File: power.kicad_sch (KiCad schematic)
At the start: 90 parts, among them J6 Molex_Nano-Fit_1x2_105309-2202, Q1 BSS138-7-F, Q2 SI7613DN-T1-GE3, Q3 BSS138-7-F, Q4 SSM3J332R, U18 TPS56C230, U19 TPS56C230, U20 TPS3840PL30DBVR, U21 TPS564247DRLR, U22 TPS564247DRLR, U23 TLV73333PDBVT, U48 INA219AIDCNR, U49 INA219AIDCNR, U50 INA219AIDCNR

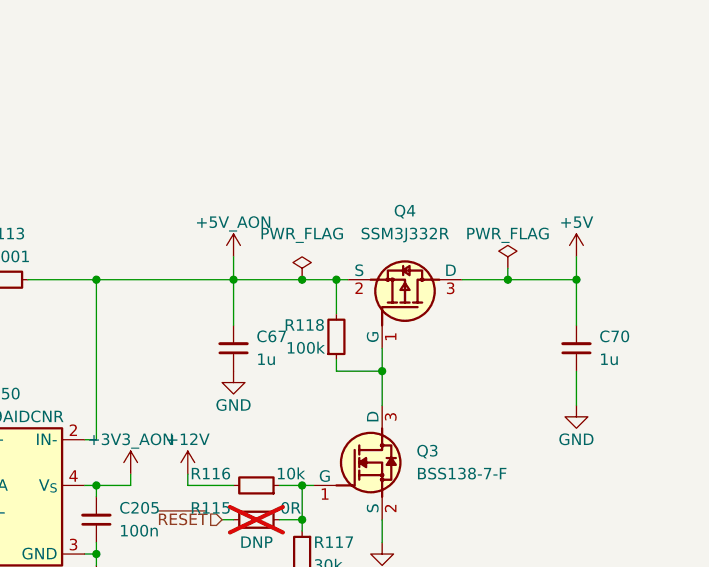
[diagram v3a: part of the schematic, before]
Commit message: [#58904] Change +5V load switch transistor to SI7613DN-T1-GE3
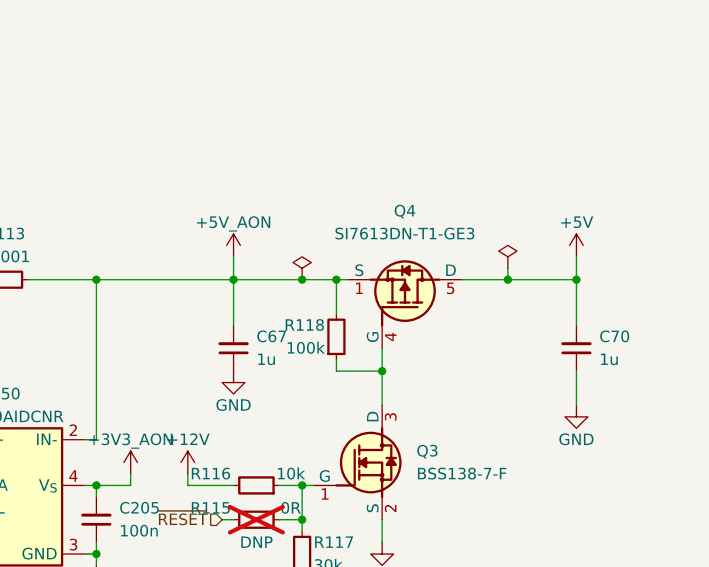
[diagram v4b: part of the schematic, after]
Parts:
- removed Q4: SSM3J332R, antmicro-footprints:SOT-23-3, symbol antmicroTransistorsFETsMOSFETsSingle:SSM3J332R
- added Q4: SI7613DN-T1-GE3, antmicro-footprints:Vishay_PowerPAK_1212-8_Single, symbol antmicroTransistorsFETsMOSFETsSingle:SI7613DN-T1-GE3
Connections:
- net +5V: now also Q4.5 (D)
- net +5V_AON: now also Q4.1 (S), Q4.2 (S), Q4.3 (S)
- net at Q3.3 (D), R118.1: now also Q4.4 (G)
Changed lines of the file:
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@@
     )
     (property "Value" "PWR_FLAG" (at 386.08 50.8 0)
-      (effects (font (size 1.27 1.27)))
+      (effects (font (size 1.27 1.27)) hide)
     )
     (property "Footprint" "" (at 386.08 54.61 0)
@@
     )
     (property "Value" "PWR_FLAG" (at 363.22 50.8 0)
-      (effects (font (size 1.27 1.27)))
+      (effects (font (size 1.27 1.27)) hide)
     )
     (property "Footprint" "" (at 363.22 55.88 0)
@@
     )
   )
+  (symbol (lib_id "antmicroTransistorsFETsMOSFETsSingle:SI7613DN-T1-GE3") (at 372.11 63.5 270) (mirror x) (unit 1)
+    (in_bom yes) (on_board yes) (dnp no) (fields_autoplaced)
+    (property "Reference" "Q4" (at 374.65 48.26 90)
+      (effects (font (size 1.27 1.27) (thickness 0.15)))
+    )
+    (property "Value" "SI7613DN-T1-GE3" (at 374.65 50.8 90)
+      (effects (font (size 1.27 1.27) (thickness 0.15)) hide)
+    )
+    (property "Footprint" "antmicro-footprints:Vishay_PowerPAK_1212-8_Single" (at 373.38 48.26 0)
+      (effects (font (size 1.27 1.27) (thickness 0.15)) (justify left bottom) hide)
+    )
+    (property "Datasheet" "https://www.vishay.com/docs/64809/si7613dn.pdf" (at 370.84 48.26 0)
+      (effects (font (size 1.27 1.27) (thickness 0.15)) (justify left bottom) hide)
+    )
+    (property "MPN" "SI7613DN-T1-GE3" (at 374.65 50.8 90)
+      (effects (font (size 1.27 1.27) (thickness 0.15)))
+    )
+    (property "Manufacturer" "Vishay" (at 364.49 48.26 0)
+      (effects (font (size 1.27 1.27) (thickness 0.15)) (justify left bottom) hide)
+    )
+    (property "Author" "Antmicro" (at 361.95 48.26 0)
+      (effects (font (size 1.27 1.27) (thickness 0.15)) (justify left bottom) hide)
+    )
+    (property "License" "Apache-2.0" (at 359.41 48.26 0)
+      (effects (font (size 1.27 1.27) (thickness 0.15)) (justify left bottom) hide)
+    )
+    (pin "5")
+    (pin "4")
+    (pin "3")
+    (pin "1")
+    (pin "2")
+    (instances
+      (project "com-express-7-baseboard"
+        (path "/1b8c34da-dad5-4b0b-8c4b-45db766c4dfa/9e43a8fe-5590-4346-856e-e8b6e5166965"
+          (reference "Q4") (unit 1)
+        )
+      )
+    )
+  )
   (symbol (lib_id "antmicroPowerMeasurement:INA219AIDCNR") (at 323.85 73.66 0) (unit 1)
     (in_bom yes) (on_board yes) (dnp no)
@@
         )
       )
-    )
-  )
-  (symbol (lib_id "antmicroTransistorsFETsMOSFETsSingle:SSM3J332R") (at 372.11 63.5 270) (mirror x) (unit 1)
-    (in_bom yes) (on_board yes) (dnp no) (fields_autoplaced)
-    (property "Reference" "Q4" (at 374.65 48.26 90)
-      (effects (font (size 1.27 1.27) (thickness 0.15)))
-    )
-    (property "Value" "SSM3J332R" (at 374.65 50.8 90)
-      (effects (font (size 1.27 1.27) (thickness 0.15)))
-    )
-    (property "Footprint" "antmicro-footprints:SOT-23-3" (at 367.03 49.53 0)
-      (effects (font (size 1.27 1.27) (thickness 0.15)) (justify left bottom) hide)
-    )
-    (property "Datasheet" "https://www.mouser.com/datasheet/2/408/SSM3J332R_datasheet_en_20181015-1150575.pdf" (at 364.49 49.53 0)
-      (effects (font (size 1.27 1.27) (thickness 0.15)) (justify left bottom) hide)
-    )
-    (property "MPN" "SSM3J332R,LF" (at 361.95 49.53 0)
-      (effects (font (size 1.27 1.27) (thickness 0.15)) (justify left bottom) hide)
-    )
-    (property "Manufacturer" "Toshiba" (at 359.41 49.53 0)
-      (effects (font (size 1.27 1.27) (thickness 0.15)) (justify left bottom) hide)
-    )
-    (property "Author" "Antmicro" (at 356.87 49.53 0)
-      (effects (font (size 1.27 1.27) (thickness 0.15)) (justify left bottom) hide)
-    )
-    (property "License" "Apache-2.0" (at 354.33 49.53 0)
-      (effects (font (size 1.27 1.27) (thickness 0.15)) (justify left bottom) hide)
-    )
-    (pin "1")
-    (pin "3")
-    (pin "2")
-    (instances
-      (project "com-express-7-baseboard"
-        (path "/1b8c34da-dad5-4b0b-8c4b-45db766c4dfa/9e43a8fe-5590-4346-856e-e8b6e5166965"
-          (reference "Q4") (unit 1)
-        )
-      )

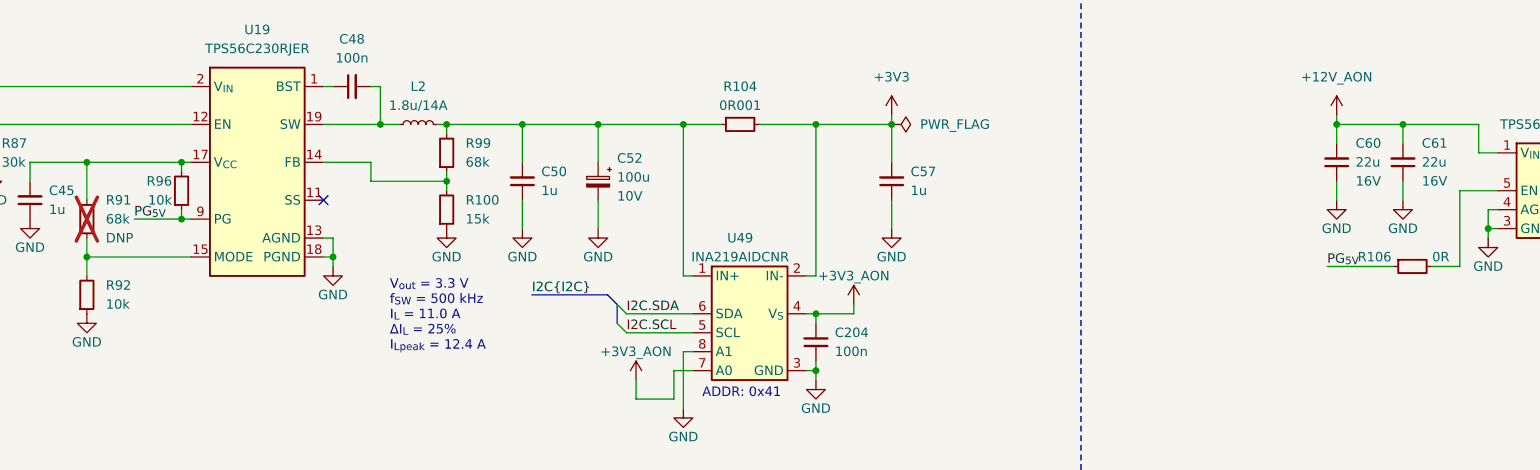
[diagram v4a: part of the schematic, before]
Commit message: [#58904] Fix DRC
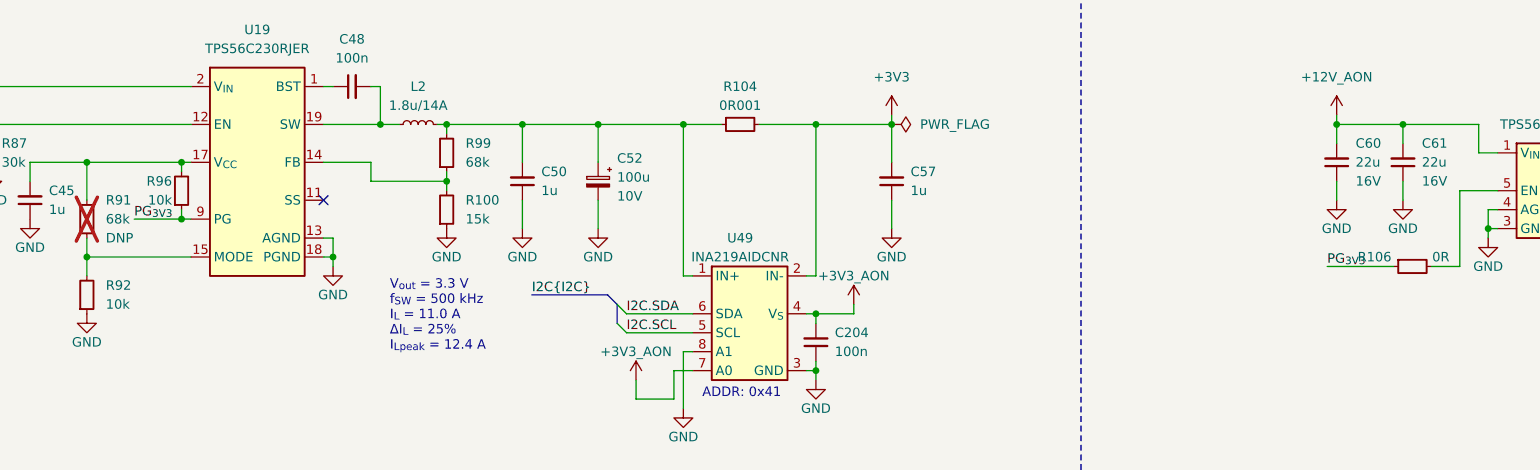
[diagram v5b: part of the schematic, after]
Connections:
- net PG_{5V} renamed PG_{3V3}
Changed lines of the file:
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@@
     (effects (font (size 1.27 1.27)) (justify left bottom))
   )
-  (label "PG_{5V}" (at 256.54 149.86 0) (fields_autoplaced)
+  (label "PG_{3V3}" (at 256.54 149.86 0) (fields_autoplaced)
     (effects (font (size 1.27 1.27)) (justify left bottom))
   )
@@
     (effects (font (size 1.27 1.27)) (justify left bottom))
   )
-  (label "PG_{5V}" (at 96.52 143.51 0) (fields_autoplaced)
+  (label "PG_{3V3}" (at 96.52 143.51 0) (fields_autoplaced)
     (effects (font (size 1.27 1.27)) (justify left bottom))
   )

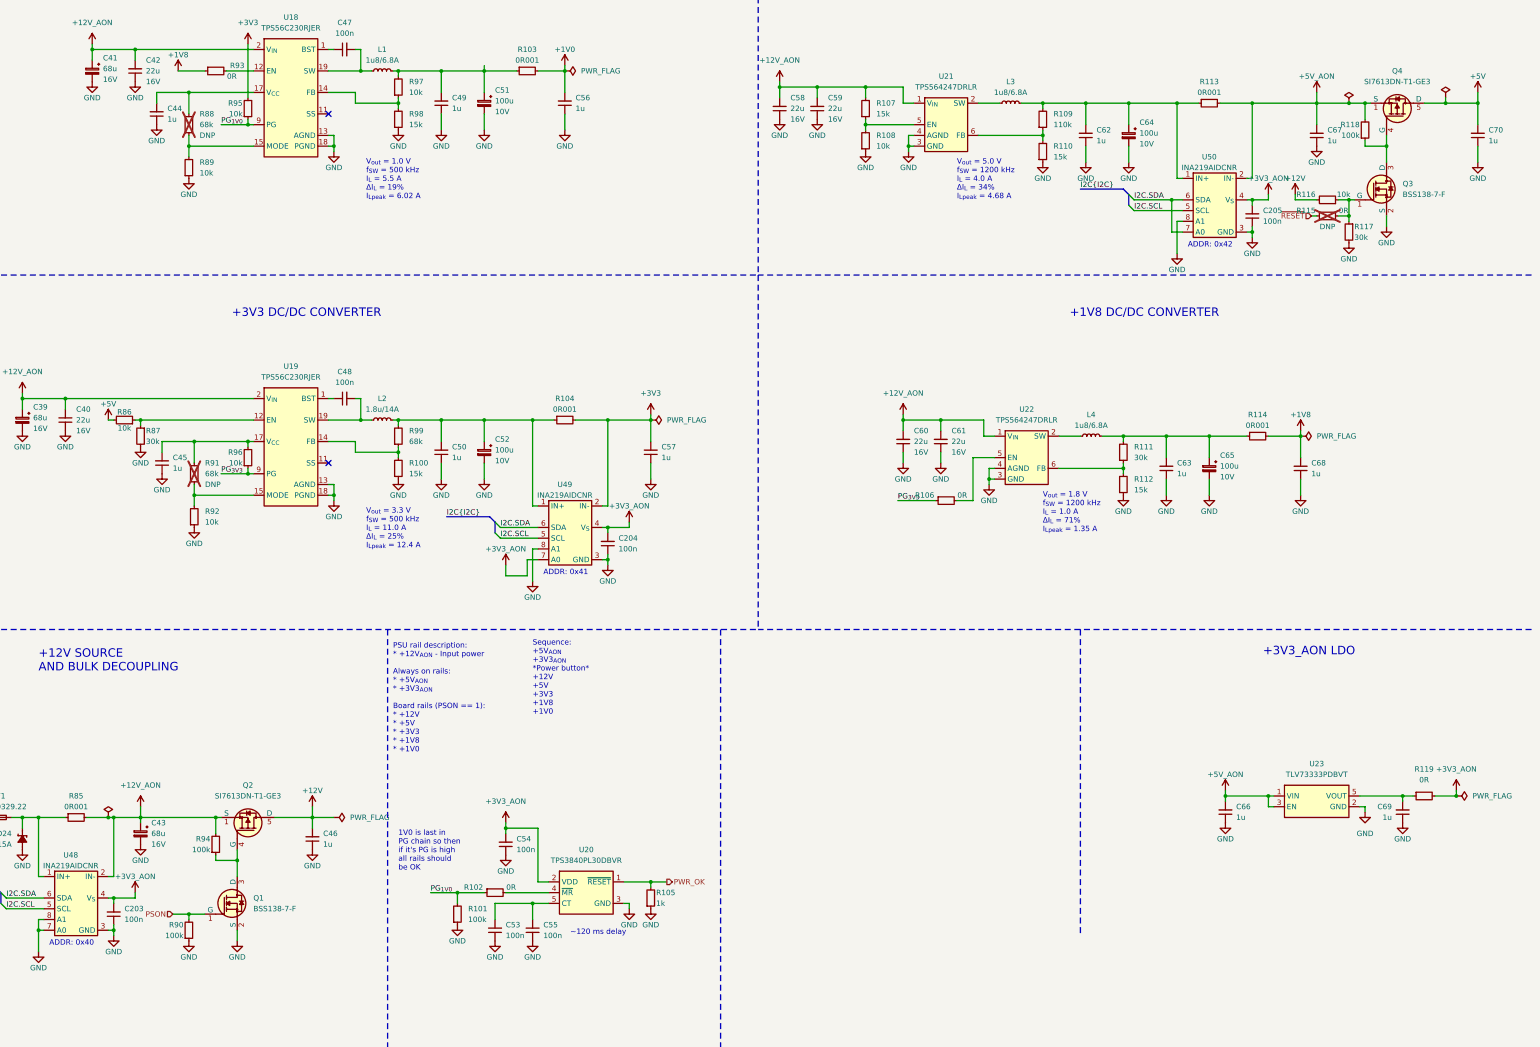
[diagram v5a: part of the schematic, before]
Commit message: Update components from the library
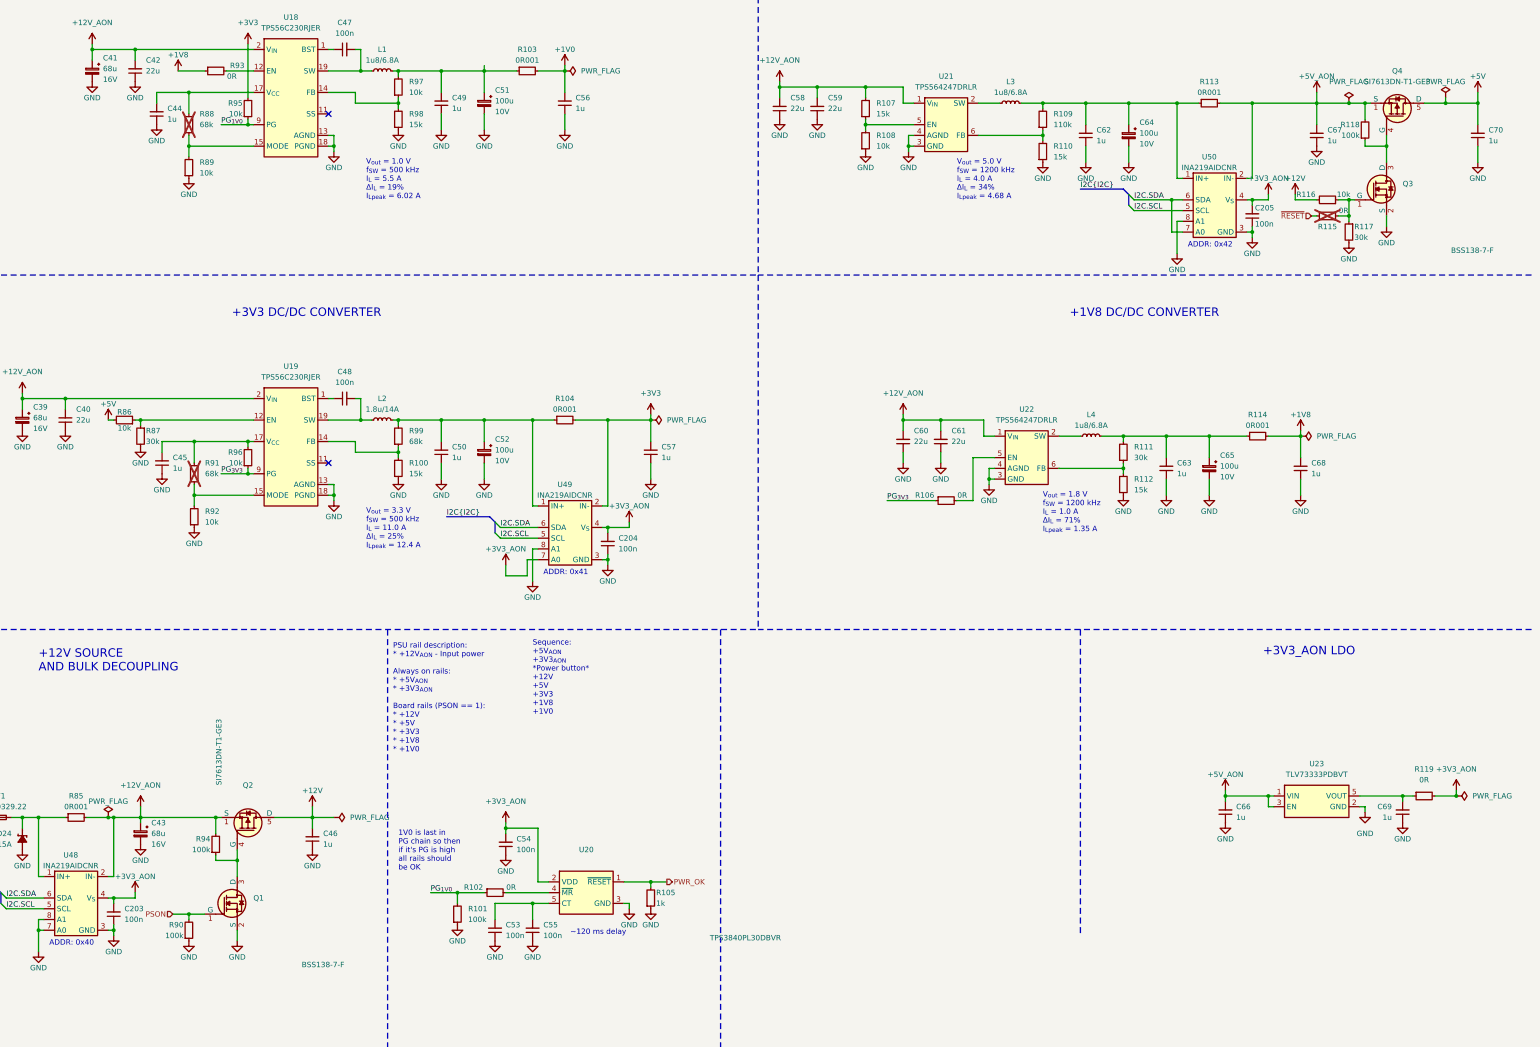
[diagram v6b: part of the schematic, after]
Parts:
- C203, C204, C205, C39, C40, C41, C42, C43, C44, C45, C46, C47, C48, C49, C50, C51, C52, C53, C54, C55, C56, C57, C58, C59, C60, C61, C62, C63, C64, C65, C66, C67, C68, C69, C70, D24, L1, L2, L3, L4, R100, R101, R102, R103, R104, R105, R106, R107, R108, R109, R110, R111, R112, R113, R114, R116, R117, R118, R119, R85, R86, R87, R89, R90, R92, R93, R94, R95, R96, R97, R98, R99: Public (none) -> False
- R115, R88, R91: DNP DNP -> (none); Public (none) -> False
- U18, U19: footprint antmicro-footprints:QFN-20-1EP_3x3mm_P0.45mm -> antmicro-footprints:QFN-20-1EP_3x3mm_P0.45mm_TPS56xxxx
- U21, U22: Manufcaturer Texas Instruments -> (none)

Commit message: [#65447] Fix rotated LEDs, overlapping text and symbols, add rules
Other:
- moved on the sheet: C70, R90
